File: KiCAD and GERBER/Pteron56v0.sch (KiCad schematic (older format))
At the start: 129 parts, among them SW1 SW_PUSH, SW10 SW_PUSH, SW11 SW_PUSH, SW12 SW_PUSH, SW13 SW_PUSH, SW14 SW_PUSH, SW15 SW_PUSH, SW16 SW_PUSH, SW17 SW_PUSH, SW18 SW_PUSH, SW19 SW_PUSH, SW2 SW_PUSH, SW20 SW_PUSH, SW21 SW_PUSH, SW22 SW_PUSH, SW23 SW_PUSH, SW24 SW_PUSH, SW25 SW_PUSH, SW26 SW_PUSH, SW27 SW_PUSH, SW28 SW_PUSH, SW29 SW_PUSH, SW3 SW_PUSH, SW30 SW_PUSH, SW31 SW_PUSH, SW32 SW_PUSH, SW33 SW_PUSH, SW34 SW_PUSH, SW35 SW_PUSH, SW36 SW_PUSH, SW37 SW_PUSH, SW38 SW_PUSH, SW39 SW_PUSH, SW4 SW_PUSH, SW40 SW_PUSH, SW41 SW_PUSH, SW42 SW_PUSH, SW43 SW_PUSH, SW44 SW_PUSH, SW45 SW_PUSH, SW46 SW_PUSH, SW47 SW_PUSH, SW48 SW_PUSH, SW49 SW_PUSH, SW5 SW_PUSH, SW50 SW_PUSH, SW51 SW_PUSH, SW52 SW_PUSH, SW53 SW_PUSH, SW54 SW_PUSH, SW55 SW_PUSH, SW56 SW_PUSH, SW57 SW_PUSH, SW6 SW_PUSH, SW7 SW_PUSH, SW8 SW_PUSH, SW9 SW_PUSH, U1 ProMicro, U2 ATMEGA32U4, X1 XTAL_GND

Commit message: add split wiring for standard Pteron56v0
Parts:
- removed C1, C2: 22p, symbol Device:C_Small
- removed C3, C4, C5, C6, C7: .1u, symbol Device:C_Small
- removed C8: 1u, symbol Device:C_Small
- removed D29, D30, D31, D32, D33, D34, D35, D36, D37, D38, D39, D40, D41, D42, D43, D44, D45, D46, D47, D48, D49, D50, D51, D52, D53, D54, D55, D56: 1N4148, Diode_THT:D_DO-35_SOD27_P7.62mm_Horizontal, symbol Diode:1N4148
- removed J?: USB_mini_micro_B, symbol keyboard_parts:USB_mini_micro_B
- removed R1, R2: 10k, symbol Device:R
- removed R3, R4: 22, symbol Device:R
- removed SW29, SW30, SW31, SW32, SW33, SW34, SW35, SW36, SW37, SW38, SW39, SW40, SW41, SW42, SW43, SW44, SW45, SW46, SW47, SW48, SW49, SW50, SW51, SW52, SW53, SW54, SW55, SW56: SW_PUSH, Keyboard parts:Mx_Alps_100, symbol keyboard_parts:SW_PUSH
- removed SW57: SW_PUSH, symbol keyboard_parts:SW_PUSH
- removed U2: ATMEGA32U4, symbol keyboard_parts:ATMEGA32U4
- removed X1: XTAL_GND, symbol keyboard_parts:XTAL_GND
- added J1, J2: AudioJack4, Connector_Audio:Jack_3.5mm_PJ320D_Horizontal, symbol Connector:AudioJack4
- D1, D10, D11, D12, D13, D14, D15, D16, D17, D18, D19, D2, D20, D21, D22, D23, D24, D25, D26, D27, D28, D3, D4, D5, D6, D7, D8, D9: footprint Diode_THT:D_DO-35_SOD27_P7.62mm_Horizontal -> Keebio-Parts:Diode-dual
- SW1, SW10, SW11, SW12, SW13, SW14, SW15, SW16, SW17, SW18, SW19, SW2, SW20, SW21, SW22, SW23, SW24, SW25, SW26, SW27, SW28, SW3, SW4, SW5, SW6, SW7, SW8, SW9: footprint Keyboard parts:Mx_Alps_100 -> Keebio-Parts:Hybrid_PCB_100H_Dual_hole
- U1: footprint Keyboard parts:Pro_Micro -> promicro:ProMicro
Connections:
- net labels added: Serial
- net labels removed: Col10, Col11, Col6, Col7, Col8, Col9
- wire segments 346 -> 154

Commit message: split36 version
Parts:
- removed D1, D2, D3, D4, D5: 1N4148, Keebio-Parts:Diode-dual, symbol Diode:1N4148
- removed SW1, SW2, SW3, SW4, SW5: SW_PUSH, Keebio-Parts:Hybrid_PCB_100H_Dual_hole, symbol keyboard_parts:SW_PUSH
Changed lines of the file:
@@
 Comment4 ""
 $EndDescr
-Text Label 750  4000 0    50   ~ 0
-Col0
 Text Label 1400 4000 0    50   ~ 0
 Col1
@@
 Wire Wire Line
 	1400 1150 1400 1750
-$Comp
-L Diode:1N4148 D4
-U 1 1 6098501B
-P 900 3000
-F 0 "D4" H 900 3217 50  0000 C CNN
-F 1 "1N4148" H 900 3126 50  0000 C CNN
-F 2 "Keebio-Parts:Diode-dual" H 900 2825 50  0001 C CNN
-F 3 "https://assets.nexperia.com/documents/data-sheet/1N4148_1N4448.pdf" H 900 3000 50  0001 C CNN
-	1    900  3000
-	1    0    0    -1
-$EndComp
-Wire Wire Line
-	1200 2750 1200 3000
-$Comp
-L keyboard_parts:SW_PUSH SW4
-U 1 1 60985022
-P 900 2750
-F 0 "SW4" H 900 3005 50  0000 C CNN
-F 1 "SW_PUSH" H 900 2914 50  0000 C CNN
-F 2 "Keebio-Parts:Hybrid_PCB_100H_Dual_hole" H 900 2750 60  0001 C CNN
-F 3 "" H 900 2750 60  0000 C CNN
-	1    900  2750
-	1    0    0    -1
-$EndComp
-Wire Wire Line
-	1200 3000 1050 3000
-Wire Wire Line
-	600  2450 1250 2450
-$Comp
-L Diode:1N4148 D3
-U 1 1 6098502A
-P 900 2400
-F 0 "D3" H 900 2617 50  0000 C CNN
-F 1 "1N4148" H 900 2526 50  0000 C CNN
-F 2 "Keebio-Parts:Diode-dual" H 900 2225 50  0001 C CNN
-F 3 "https://assets.nexperia.com/documents/data-sheet/1N4148_1N4448.pdf" H 900 2400 50  0001 C CNN
-	1    900  2400
-	1    0    0    -1
-$EndComp
-Wire Wire Line
-	1200 2150 1200 2400
-$Comp
-L keyboard_parts:SW_PUSH SW3
-U 1 1 60985031
-P 900 2150
-F 0 "SW3" H 900 2405 50  0000 C CNN
-F 1 "SW_PUSH" H 900 2314 50  0000 C CNN
-F 2 "Keebio-Parts:Hybrid_PCB_100H_Dual_hole" H 900 2150 60  0001 C CNN
-F 3 "" H 900 2150 60  0000 C CNN
-	1    900  2150
-	1    0    0    -1
-$EndComp
-Wire Wire Line
-	1200 2400 1050 2400
-Wire Wire Line
-	750  2400 750  3000
-Connection ~ 1250 1200
-Connection ~ 1250 600
-Wire Wire Line
-	750  1150 750  1750
-Wire Wire Line
-	600  600  1250 600
-Wire Wire Line
-	600  900  600  600
-Wire Wire Line
-	1200 1150 1050 1150
-$Comp
-L keyboard_parts:SW_PUSH SW1
-U 1 1 6091D9A9
-P 900 900
-F 0 "SW1" H 900 1155 50  0000 C CNN
-F 1 "SW_PUSH" H 900 1064 50  0000 C CNN
-F 2 "Keebio-Parts:Hybrid_PCB_100H_Dual_hole" H 900 900 60  0001 C CNN
-F 3 "" H 900 900 60  0000 C CNN
-	1    900  900
-	1    0    0    -1
-$EndComp
-Wire Wire Line
-	1200 900  1200 1150
-$Comp
-L Diode:1N4148 D1
-U 1 1 6091C810
-P 900 1150
-F 0 "D1" H 900 1367 50  0000 C CNN
-F 1 "1N4148" H 900 1276 50  0000 C CNN
-F 2 "Keebio-Parts:Diode-dual" H 900 975 50  0001 C CNN
-F 3 "https://assets.nexperia.com/documents/data-sheet/1N4148_1N4448.pdf" H 900 1150 50  0001 C CNN
-	1    900  1150
-	1    0    0    -1
-$EndComp
-Wire Wire Line
-	600  1200 1250 1200
-Wire Wire Line
-	600  1500 600  1200
-Wire Wire Line
-	1200 1750 1050 1750
-$Comp
-L keyboard_parts:SW_PUSH SW2
-U 1 1 608ADD43
-P 900 1500
-F 0 "SW2" H 900 1755 50  0000 C CNN
-F 1 "SW_PUSH" H 900 1664 50  0000 C CNN
-F 2 "Keebio-Parts:Hybrid_PCB_100H_Dual_hole" H 900 1500 60  0001 C CNN
-F 3 "" H 900 1500 60  0000 C CNN
-	1    900  1500
-	1    0    0    -1
-$EndComp
-Wire Wire Line
-	1200 1500 1200 1750
-$Comp
-L Diode:1N4148 D2
-U 1 1 608ADD08
-P 900 1750
-F 0 "D2" H 900 1967 50  0000 C CNN
-F 1 "1N4148" H 900 1876 50  0000 C CNN
-F 2 "Keebio-Parts:Diode-dual" H 900 1575 50  0001 C CNN
-F 3 "https://assets.nexperia.com/documents/data-sheet/1N4148_1N4448.pdf" H 900 1750 50  0001 C CNN
-	1    900  1750
-	1    0    0    -1
-$EndComp
 Wire Wire Line
 	1250 1850 1900 1850
@@
 $EndComp
 Wire Wire Line
-	600  2450 600  2750
-Wire Wire Line
-	600  2150 600  1850
-Wire Wire Line
-	600  1850 1250 1850
-Wire Wire Line
-	750  1750 750  2400
-Connection ~ 750  1750
-Connection ~ 750  2400
-Wire Wire Line
 	1400 2400 1400 1750
 Connection ~ 1400 2400
@@
 Connection ~ 3350 2400
 Connection ~ 3350 1750
-Connection ~ 1250 1850
-Connection ~ 1250 2450
 Connection ~ 1900 600
 Connection ~ 1900 1200
@@
 	1    0    0    -1
 $EndComp
-$Comp
-L Diode:1N4148 D5
-U 1 1 60EDB4C1
-P 900 3600
-F 0 "D5" H 900 3817 50  0000 C CNN
-F 1 "1N4148" H 900 3726 50  0000 C CNN
-F 2 "Keebio-Parts:Diode-dual" H 900 3425 50  0001 C CNN
-F 3 "https://assets.nexperia.com/documents/data-sheet/1N4148_1N4448.pdf" H 900 3600 50  0001 C CNN
-	1    900  3600
-	1    0    0    -1
-$EndComp
-Wire Wire Line
-	1200 3350 1200 3600
-$Comp
-L keyboard_parts:SW_PUSH SW5
-U 1 1 60EDC258
-P 900 3350
-F 0 "SW5" H 900 3605 50  0000 C CNN
-F 1 "SW_PUSH" H 900 3514 50  0000 C CNN
-F 2 "Keebio-Parts:Hybrid_PCB_100H_Dual_hole" H 900 3350 60  0001 C CNN
-F 3 "" H 900 3350 60  0000 C CNN
-	1    900  3350
-	1    0    0    -1
-$EndComp
-Wire Wire Line
-	1200 3600 1050 3600
 Wire Wire Line
 	1850 3600 1700 3600
@@
 $EndComp
 Wire Wire Line
-	600  3350 600  3050
-Wire Wire Line
-	600  3050 1250 3050
-Wire Wire Line
 	1250 3350 1250 3050
-Connection ~ 1250 3050
 Wire Wire Line
 	1250 3050 1900 3050
@@
 Connection ~ 1400 3000
 Wire Wire Line
-	750  3600 750  3000
-Connection ~ 750  3000
-Wire Wire Line
-	750  3600 750  4000
-Connection ~ 750  3600
-Wire Wire Line
 	1400 3600 1400 4000

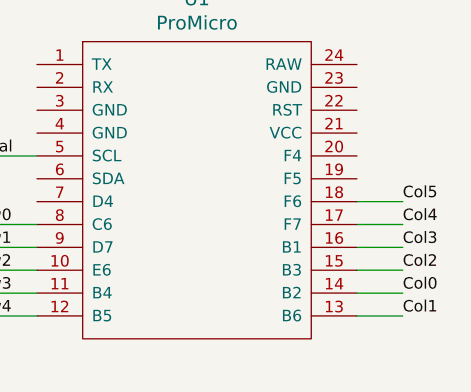
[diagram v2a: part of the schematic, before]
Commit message: finalised the design, add mounting holes
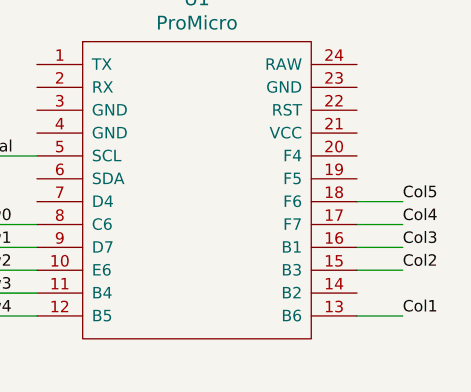
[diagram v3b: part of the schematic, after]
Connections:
- net Col0: no longer names the net of U1.14 (B2)
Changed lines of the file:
@@
 Text Label 8100 5650 0    50   ~ 0
 Row4
-Text Label 10000 5550 0    50   ~ 0
-Col0
 Text Label 10000 5650 0    50   ~ 0
 Col1
@@
 Wire Wire Line
 	9800 5650 10000 5650
-Wire Wire Line
-	9800 5550 10000 5550
 Text Label 4000 4000 0    50   ~ 0
 Col5

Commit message: added gerber files
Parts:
- added H1, H2, H3, H4, H5, H6, H7: MountingHole, MountingHole:MountingHole_3.2mm_M3, symbol Mechanical:MountingHole
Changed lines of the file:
@@
 Wire Wire Line
 	6850 5600 7050 5600
+$Comp
+L Mechanical:MountingHole H1
+U 1 1 60759BE2
+P 10100 6000
+F 0 "H1" H 10200 6046 50  0000 L CNN
+F 1 "MountingHole" H 10200 5955 50  0000 L CNN
+F 2 "MountingHole:MountingHole_3.2mm_M3" H 10100 6000 50  0001 C CNN
+F 3 "~" H 10100 6000 50  0001 C CNN
+	1    10100 6000
+	1    0    0    -1
+$EndComp
+$Comp
+L Mechanical:MountingHole H3
+U 1 1 60759F7C
+P 10400 6000
+F 0 "H3" H 10500 6046 50  0000 L CNN
+F 1 "MountingHole" H 10500 5955 50  0000 L CNN
+F 2 "MountingHole:MountingHole_3.2mm_M3" H 10400 6000 50  0001 C CNN
+F 3 "~" H 10400 6000 50  0001 C CNN
+	1    10400 6000
+	1    0    0    -1
+$EndComp
+$Comp
+L Mechanical:MountingHole H5
+U 1 1 6075A135
+P 10700 6000
+F 0 "H5" H 10800 6046 50  0000 L CNN
+F 1 "MountingHole" H 10800 5955 50  0000 L CNN
+F 2 "MountingHole:MountingHole_3.2mm_M3" H 10700 6000 50  0001 C CNN
+F 3 "~" H 10700 6000 50  0001 C CNN
+	1    10700 6000
+	1    0    0    -1
+$EndComp
+$Comp
+L Mechanical:MountingHole H6
+U 1 1 6075A3BD
+P 10700 6250
+F 0 "H6" H 10800 6296 50  0000 L CNN
+F 1 "MountingHole" H 10800 6205 50  0000 L CNN
+F 2 "MountingHole:MountingHole_3.2mm_M3" H 10700 6250 50  0001 C CNN
+F 3 "~" H 10700 6250 50  0001 C CNN
+	1    10700 6250
+	1    0    0    -1
+$EndComp
+$Comp
+L Mechanical:MountingHole H4
+U 1 1 6075A694
+P 10400 6250
+F 0 "H4" H 10500 6296 50  0000 L CNN
+F 1 "MountingHole" H 10500 6205 50  0000 L CNN
+F 2 "MountingHole:MountingHole_3.2mm_M3" H 10400 6250 50  0001 C CNN
+F 3 "~" H 10400 6250 50  0001 C CNN
+	1    10400 6250
+	1    0    0    -1
+$EndComp
+$Comp
+L Mechanical:MountingHole H2
+U 1 1 6075A93C
+P 10100 6250
+F 0 "H2" H 10200 6296 50  0000 L CNN
+F 1 "MountingHole" H 10200 6205 50  0000 L CNN
+F 2 "MountingHole:MountingHole_3.2mm_M3" H 10100 6250 50  0001 C CNN
+F 3 "~" H 10100 6250 50  0001 C CNN
+	1    10100 6250
+	1    0    0    -1
+$EndComp
+$Comp
+L Mechanical:MountingHole H7
+U 1 1 607A62BA
+P 10100 6450
+F 0 "H7" H 10200 6496 50  0000 L CNN
+F 1 "MountingHole" H 10200 6405 50  0000 L CNN
+F 2 "MountingHole:MountingHole_3.2mm_M3" H 10100 6450 50  0001 C CNN
+F 3 "~" H 10100 6450 50  0001 C CNN
+	1    10100 6450
+	1    0    0    -1
+$EndComp
 $EndSCHEMATC

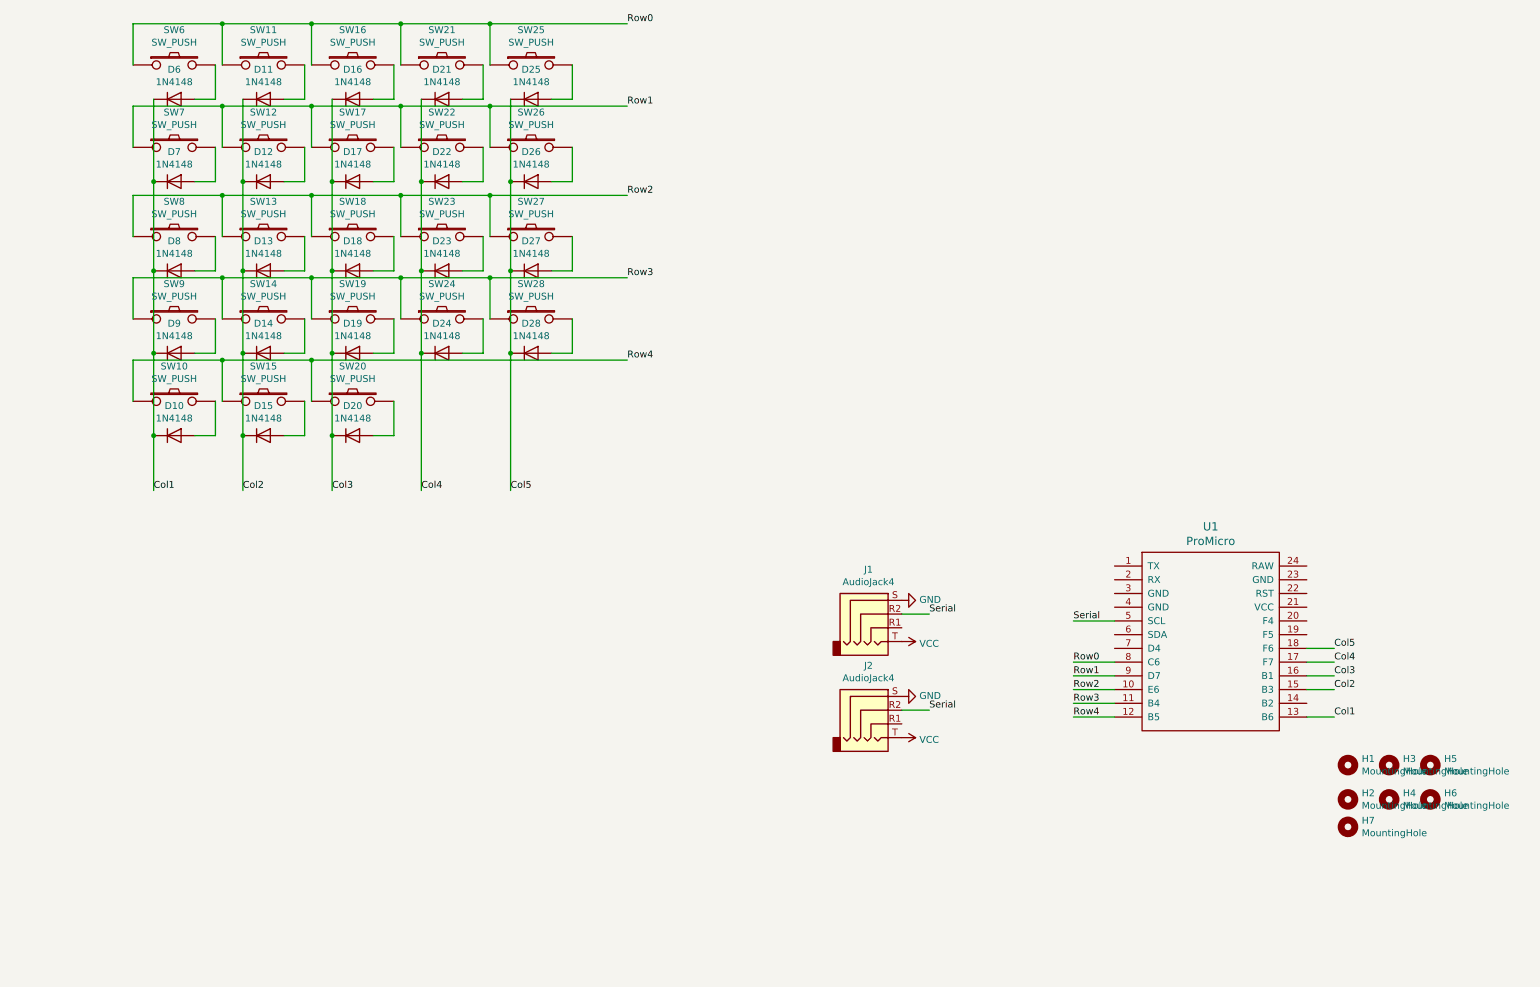
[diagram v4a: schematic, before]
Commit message: remove top row.
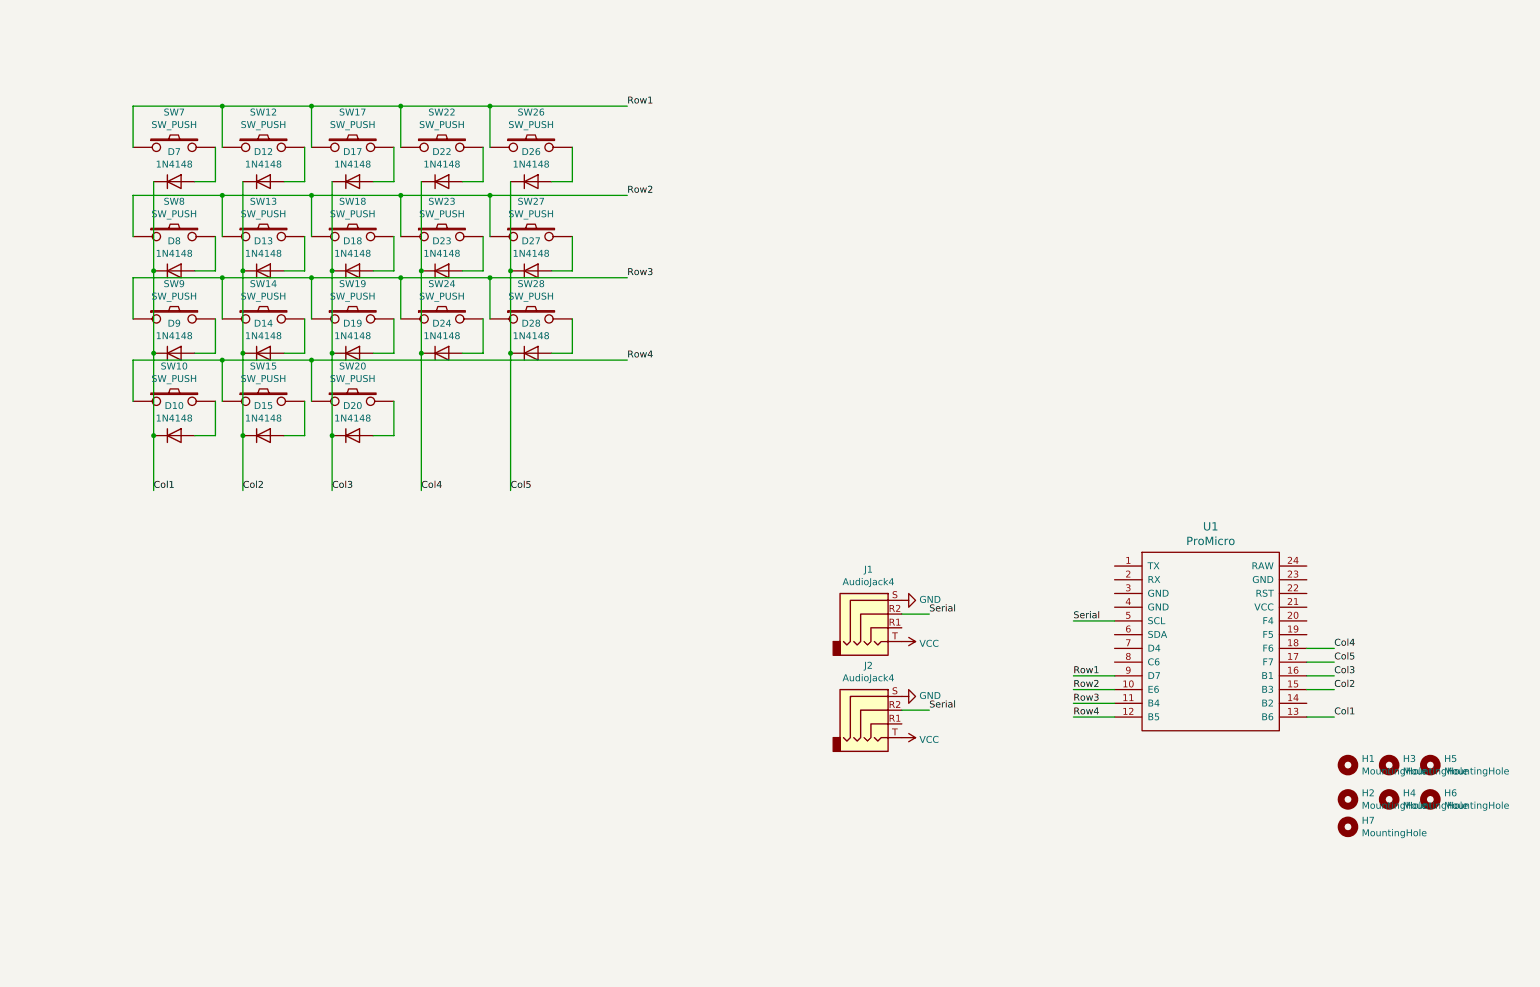
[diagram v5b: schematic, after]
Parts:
- removed D11, D16, D21, D25, D6: 1N4148, Keebio-Parts:Diode-dual, symbol Diode:1N4148
- removed SW11, SW16, SW21, SW25, SW6: SW_PUSH, Keebio-Parts:Hybrid_PCB_100H_Dual_hole, symbol keyboard_parts:SW_PUSH
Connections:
- net Col4: now also U1.18 (F6); no longer U1.17 (F7)
- net Col5: now also U1.17 (F7); no longer U1.18 (F6)
- net Row0: no longer names the net of U1.8 (C6)
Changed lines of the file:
@@
 Text Label 3350 4000 0    50   ~ 0
 Col4
-Text Label 8100 5250 0    50   ~ 0
-Row0
 Text Label 8100 5350 0    50   ~ 0
 Row1
@@
 Text Label 10000 5350 0    50   ~ 0
 Col3
+Text Label 10000 5150 0    50   ~ 0
+Col4
 Text Label 10000 5250 0    50   ~ 0
-Col4
-Text Label 10000 5150 0    50   ~ 0
 Col5
 Wire Wire Line
@@
 Wire Wire Line
 	1250 1200 1900 1200
-$Comp
-L Diode:1N4148 D6
-U 1 1 60963573
-P 1550 1150
-F 0 "D6" H 1550 1367 50  0000 C CNN
-F 1 "1N4148" H 1550 1276 50  0000 C CNN
-F 2 "Keebio-Parts:Diode-dual" H 1550 975 50  0001 C CNN
-F 3 "https://assets.nexperia.com/documents/data-sheet/1N4148_1N4448.pdf" H 1550 1150 50  0001 C CNN
-	1    1550 1150
-	1    0    0    -1
-$EndComp
-Wire Wire Line
-	1850 900  1850 1150
-$Comp
-L keyboard_parts:SW_PUSH SW6
-U 1 1 6096357E
-P 1550 900
-F 0 "SW6" H 1550 1155 50  0000 C CNN
-F 1 "SW_PUSH" H 1550 1064 50  0000 C CNN
-F 2 "Keebio-Parts:Hybrid_PCB_100H_Dual_hole" H 1550 900 60  0001 C CNN
-F 3 "" H 1550 900 60  0000 C CNN
-	1    1550 900
-	1    0    0    -1
-$EndComp
-Wire Wire Line
-	1850 1150 1700 1150
-Wire Wire Line
-	1250 900  1250 600
-Wire Wire Line
-	1250 600  1900 600
-Wire Wire Line
-	1400 1150 1400 1750
 Wire Wire Line
 	1250 1850 1900 1850
@@
 $EndComp
 Wire Wire Line
-	2050 1150 2050 1750
-Wire Wire Line
-	1900 600  2550 600
-Wire Wire Line
-	1900 900  1900 600
-Wire Wire Line
-	2500 1150 2350 1150
-$Comp
-L keyboard_parts:SW_PUSH SW11
-U 1 1 609D6518
-P 2200 900
-F 0 "SW11" H 2200 1155 50  0000 C CNN
-F 1 "SW_PUSH" H 2200 1064 50  0000 C CNN
-F 2 "Keebio-Parts:Hybrid_PCB_100H_Dual_hole" H 2200 900 60  0001 C CNN
-F 3 "" H 2200 900 60  0000 C CNN
-	1    2200 900
-	1    0    0    -1
-$EndComp
-Wire Wire Line
-	2500 900  2500 1150
-$Comp
-L Diode:1N4148 D11
-U 1 1 609D651F
-P 2200 1150
-F 0 "D11" H 2200 1367 50  0000 C CNN
-F 1 "1N4148" H 2200 1276 50  0000 C CNN
-F 2 "Keebio-Parts:Diode-dual" H 2200 975 50  0001 C CNN
-F 3 "https://assets.nexperia.com/documents/data-sheet/1N4148_1N4448.pdf" H 2200 1150 50  0001 C CNN
-	1    2200 1150
-	1    0    0    -1
-$EndComp
-Wire Wire Line
 	1900 1200 2550 1200
 Wire Wire Line
@@
 $EndComp
 Wire Wire Line
-	2700 1150 2700 1750
-Wire Wire Line
-	2550 600  3200 600
-Wire Wire Line
-	2550 900  2550 600
-Wire Wire Line
-	3150 1150 3000 1150
-$Comp
-L keyboard_parts:SW_PUSH SW16
-U 1 1 60A11253
-P 2850 900
-F 0 "SW16" H 2850 1155 50  0000 C CNN
-F 1 "SW_PUSH" H 2850 1064 50  0000 C CNN
-F 2 "Keebio-Parts:Hybrid_PCB_100H_Dual_hole" H 2850 900 60  0001 C CNN
-F 3 "" H 2850 900 60  0000 C CNN
-	1    2850 900
-	1    0    0    -1
-$EndComp
-Wire Wire Line
-	3150 900  3150 1150
-$Comp
-L Diode:1N4148 D16
-U 1 1 60A1125A
-P 2850 1150
-F 0 "D16" H 2850 1367 50  0000 C CNN
-F 1 "1N4148" H 2850 1276 50  0000 C CNN
-F 2 "Keebio-Parts:Diode-dual" H 2850 975 50  0001 C CNN
-F 3 "https://assets.nexperia.com/documents/data-sheet/1N4148_1N4448.pdf" H 2850 1150 50  0001 C CNN
-	1    2850 1150
-	1    0    0    -1
-$EndComp
-Wire Wire Line
 	2550 1200 3200 1200
 Wire Wire Line
@@
 $EndComp
 Wire Wire Line
-	3350 1150 3350 1750
-Wire Wire Line
-	3200 600  3850 600
-Wire Wire Line
-	3200 900  3200 600
-Wire Wire Line
-	3800 1150 3650 1150
-$Comp
-L keyboard_parts:SW_PUSH SW21
-U 1 1 60A305BB
-P 3500 900
-F 0 "SW21" H 3500 1155 50  0000 C CNN
-F 1 "SW_PUSH" H 3500 1064 50  0000 C CNN
-F 2 "Keebio-Parts:Hybrid_PCB_100H_Dual_hole" H 3500 900 60  0001 C CNN
-F 3 "" H 3500 900 60  0000 C CNN
-	1    3500 900
-	1    0    0    -1
-$EndComp
-Wire Wire Line
-	3800 900  3800 1150
-$Comp
-L Diode:1N4148 D21
-U 1 1 60A305C2
-P 3500 1150
-F 0 "D21" H 3500 1367 50  0000 C CNN
-F 1 "1N4148" H 3500 1276 50  0000 C CNN
-F 2 "Keebio-Parts:Diode-dual" H 3500 975 50  0001 C CNN
-F 3 "https://assets.nexperia.com/documents/data-sheet/1N4148_1N4448.pdf" H 3500 1150 50  0001 C CNN
-	1    3500 1150
-	1    0    0    -1
-$EndComp
-Wire Wire Line
 	3200 1200 3850 1200
 Wire Wire Line
@@
 	1400 2400 1400 1750
 Connection ~ 1400 2400
-Connection ~ 1400 1750
 Wire Wire Line
 	2050 1750 2050 2400
-Connection ~ 2050 1750
 Connection ~ 2050 2400
 Wire Wire Line
 	2700 1750 2700 2400
-Connection ~ 2700 1750
 Connection ~ 2700 2400
 Wire Wire Line
 	3350 2400 3350 1750
 Connection ~ 3350 2400
-Connection ~ 3350 1750
-Connection ~ 1900 600
 Connection ~ 1900 1200
 Connection ~ 1900 1850
 Connection ~ 1900 2450
-Connection ~ 2550 600
 Connection ~ 2550 1200
 Connection ~ 2550 1850
 Connection ~ 2550 2450
-Connection ~ 3200 600
 Connection ~ 3200 1200
 Connection ~ 3200 1850
 Connection ~ 3200 2450
-Wire Wire Line
-	4000 1150 4000 1750
-Wire Wire Line
-	3850 900  3850 600
-Wire Wire Line
-	4450 1150 4300 1150
-$Comp
-L keyboard_parts:SW_PUSH SW25
-U 1 1 60C99C95
-P 4150 900
-F 0 "SW25" H 4150 1155 50  0000 C CNN
-F 1 "SW_PUSH" H 4150 1064 50  0000 C CNN
-F 2 "Keebio-Parts:Hybrid_PCB_100H_Dual_hole" H 4150 900 60  0001 C CNN
-F 3 "" H 4150 900 60  0000 C CNN
-	1    4150 900
-	1    0    0    -1
-$EndComp
-Wire Wire Line
-	4450 900  4450 1150
-$Comp
-L Diode:1N4148 D25
-U 1 1 60C99C9C
-P 4150 1150
-F 0 "D25" H 4150 1367 50  0000 C CNN
-F 1 "1N4148" H 4150 1276 50  0000 C CNN
-F 2 "Keebio-Parts:Diode-dual" H 4150 975 50  0001 C CNN
-F 3 "https://assets.nexperia.com/documents/data-sheet/1N4148_1N4448.pdf" H 4150 1150 50  0001 C CNN
-	1    4150 1150
-	1    0    0    -1
-$EndComp
 Wire Wire Line
 	3850 1500 3850 1200
@@
 	4000 2400 4000 1750
 Connection ~ 4000 2400
-Connection ~ 4000 1750
 $Comp
 L promicro:ProMicro U1
@@
 Text Label 4850 1850 0    50   ~ 0
 Row2
-Text Label 4850 600  0    50   ~ 0
-Row0
-Wire Wire Line
-	3850 600  4850 600
-Connection ~ 3850 600
 Wire Wire Line
 	3850 1200 4850 1200
@@
 	8100 5550 8400 5550
 Wire Wire Line
-	8100 5250 8400 5250
-Wire Wire Line
 	8400 4950 8100 4950
